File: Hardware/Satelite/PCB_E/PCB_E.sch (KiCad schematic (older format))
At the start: 15 parts, among them J1 Conn_02x02_Counter_Clockwise, J12 Conector_Expansion_CanSat, J14 Conn_01x06, J15 Conn_01x06, J2 Conn_02x02_Counter_Clockwise, J3 Conn_02x02_Counter_Clockwise, J4 Conn_02x10_Odd_Even, J5 Conn_02x10_Odd_Even, J6 Conn_02x10_Odd_Even, J7 Conn_02x10_Odd_Even, J8 Conn_01x06, M1 Spacer, M2 Spacer, M3 Spacer

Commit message: Espaciadores más largos para PCB que usan conector de expansión
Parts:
- J12: symbol AXTEC_IC:Conector_Expansion_CanSat -> PCB_E-rescue:Conector_Expansion_CanSat-AXTEC_IC
- M1, M2, M3: symbol AXTEC_IC:Spacer -> PCB_E-rescue:Spacer-AXTEC_IC; Manufacturer Part Number R30-3011002 -> R30-3011202
- MH1: symbol AXTEC_IC:MH_CanSat -> PCB_E-rescue:MH_CanSat-AXTEC_IC
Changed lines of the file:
@@
 EESchema Schematic File Version 4
 LIBS:PCB_E-cache
-EELAYER 26 0
+EELAYER 29 0
 EELAYER END
 $Descr A4 11693 8268
@@
 IO6
 $Comp
-L AXTEC_IC:MH_CanSat MH1
+L PCB_E-rescue:MH_CanSat-AXTEC_IC MH1
 U 1 1 5BC69FBC
 P 5250 4650
@@
 	8050 2150 8050 2250
 $Comp
-L AXTEC_IC:Spacer M1
+L PCB_E-rescue:Spacer-AXTEC_IC M1
 U 1 1 5C332544
 P 4400 5450
@@
 F 2 "AXTEC:Empty_Footprint" H 4300 5600 50  0001 C CNN
 F 3 "https://www.mouser.com/datasheet/2/181/R30-301-1135805.pdf" H 4400 5700 50  0001 C CNN
-F 4 "R30-3011002" H 4479 5305 50  0001 L CNN "Manufacturer Part Number"
+F 4 "R30-3011202" H 4479 5305 50  0001 L CNN "Manufacturer Part Number"
 	1    4400 5450
 	1    0    0    -1
 $EndComp
 $Comp
-L AXTEC_IC:Spacer M2
+L PCB_E-rescue:Spacer-AXTEC_IC M2
 U 1 1 5C332635
 P 5250 5450
@@
 F 2 "AXTEC:Empty_Footprint" H 5150 5600 50  0001 C CNN
 F 3 "https://www.mouser.com/datasheet/2/181/R30-301-1135805.pdf" H 5250 5700 50  0001 C CNN
-F 4 "R30-3011002" H 5329 5305 50  0001 L CNN "Manufacturer Part Number"
+F 4 "R30-3011202" H 5329 5305 50  0001 L CNN "Manufacturer Part Number"
 	1    5250 5450
 	1    0    0    -1
 $EndComp
 $Comp
-L AXTEC_IC:Spacer M3
+L PCB_E-rescue:Spacer-AXTEC_IC M3
 U 1 1 5C332687
 P 6000 5450
@@
 F 2 "AXTEC:Empty_Footprint" H 5900 5600 50  0001 C CNN
 F 3 "https://www.mouser.com/datasheet/2/181/R30-301-1135805.pdf" H 6000 5700 50  0001 C CNN
-F 4 "R30-3011002" H 6079 5305 50  0001 L CNN "Manufacturer Part Number"
+F 4 "R30-3011202" H 6079 5305 50  0001 L CNN "Manufacturer Part Number"
 	1    6000 5450
 	1    0    0    -1
@@
 $EndComp
 $Comp
-L AXTEC_IC:Conector_Expansion_CanSat J12
+L PCB_E-rescue:Conector_Expansion_CanSat-AXTEC_IC J12
 U 1 1 5C26BB39
 P 8750 2100

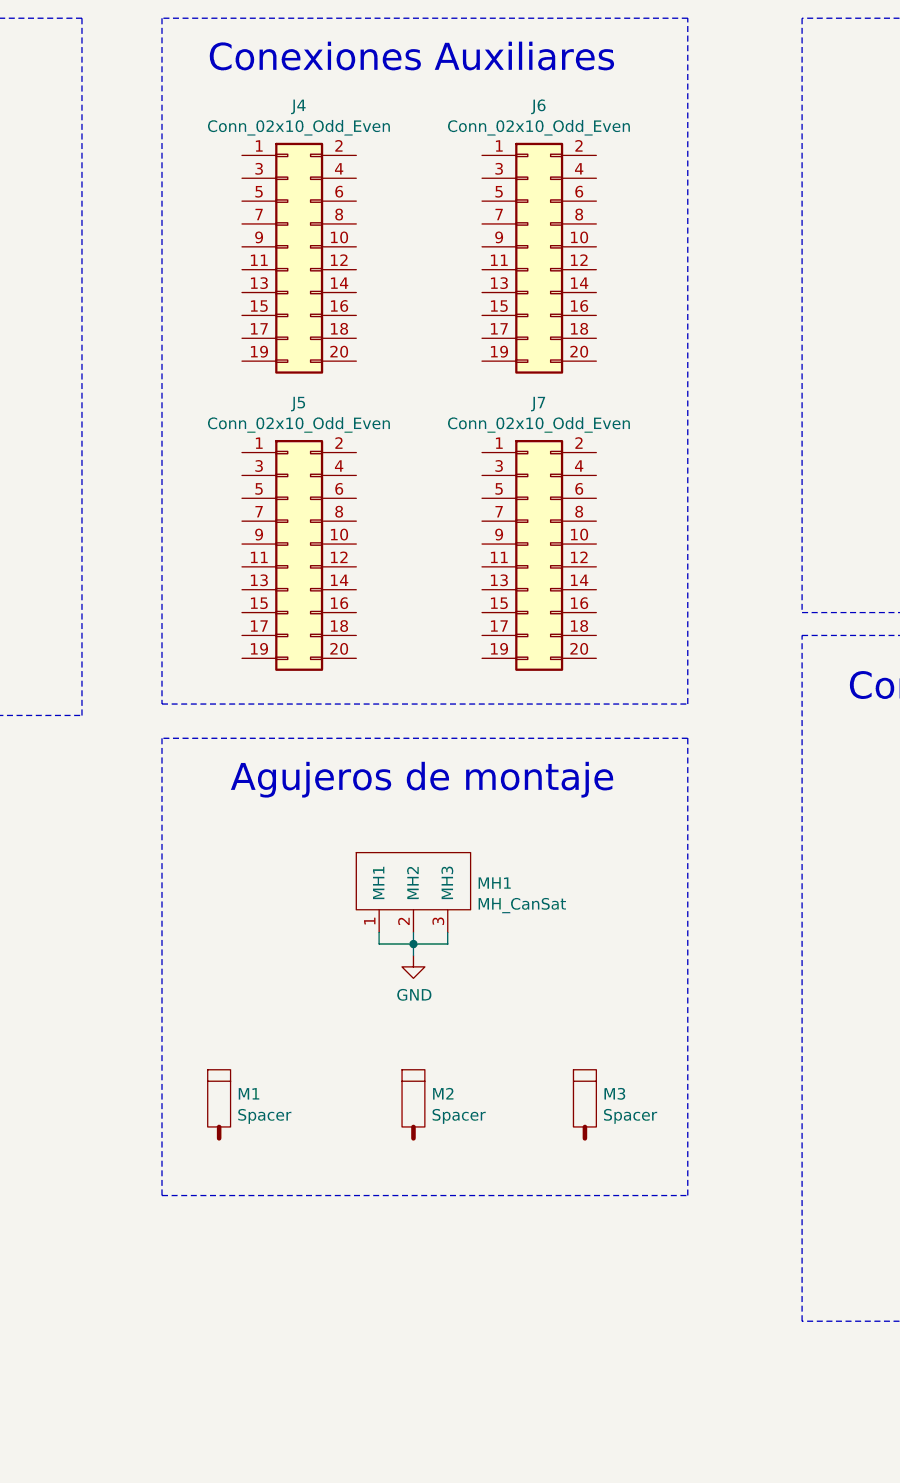
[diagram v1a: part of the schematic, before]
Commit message: Agregado más pines y corrección de distancia entre pines en PCB_E
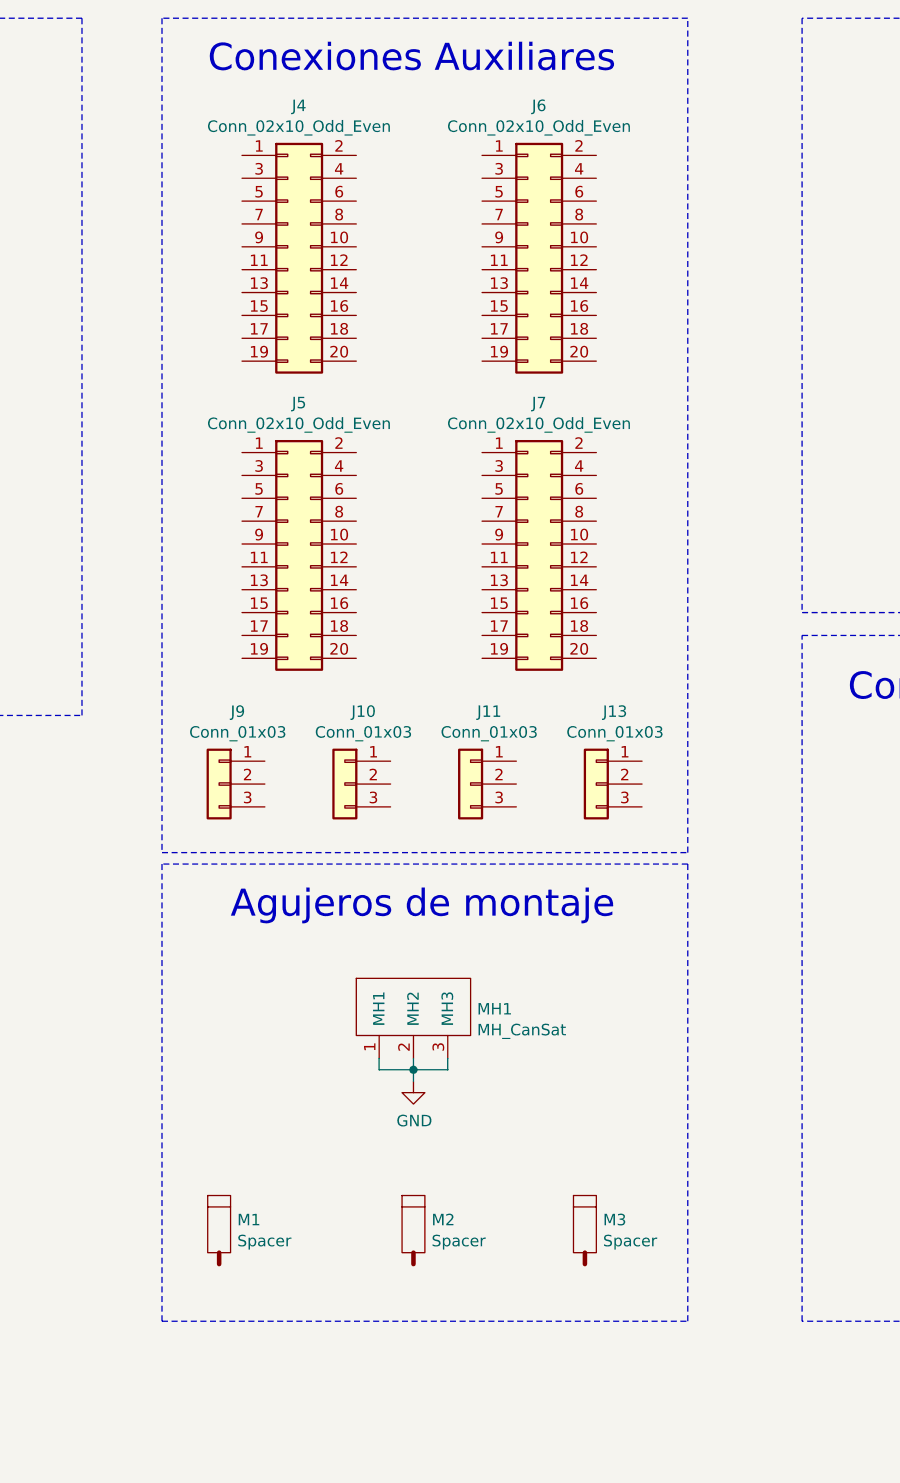
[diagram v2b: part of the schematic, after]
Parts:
- added J10, J11, J13, J9: Conn_01x03, Connector_PinHeader_2.54mm:PinHeader_1x03_P2.54mm_Vertical, symbol Connector_Generic:Conn_01x03
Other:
- moved on the sheet: M1, M2, M3, MH1
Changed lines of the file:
@@
 $EndComp
 Wire Notes Line
-	4150 750  4150 3750
-Wire Notes Line
-	4150 3750 6450 3750
-Wire Notes Line
-	6450 3750 6450 750
+	4150 750  4150 4400
+Wire Notes Line
+	4150 4400 6450 4400
+Wire Notes Line
+	6450 4400 6450 750
 Wire Notes Line
 	6450 750  4150 750
@@
 L power:GND #PWR07
 U 1 1 5BC9E797
-P 5250 4850
-F 0 "#PWR07" H 5250 4600 50  0001 C CNN
-F 1 "GND" H 5254 4676 50  0000 C CNN
-F 2 "" H 5250 4850 50  0001 C CNN
-F 3 "" H 5250 4850 50  0001 C CNN
-	1    5250 4850
+P 5250 5400
+F 0 "#PWR07" H 5250 5150 50  0001 C CNN
+F 1 "GND" H 5254 5226 50  0000 C CNN
+F 2 "" H 5250 5400 50  0001 C CNN
+F 3 "" H 5250 5400 50  0001 C CNN
+	1    5250 5400
 	1    0    0    -1
 $EndComp
@@
 L PCB_E-rescue:MH_CanSat-AXTEC_IC MH1
 U 1 1 5BC69FBC
-P 5250 4650
-F 0 "MH1" H 5528 4765 50  0000 L CNN
-F 1 "MH_CanSat" H 5528 4674 50  0000 L CNN
-F 2 "AXTEC:MH_CanSat" H 5250 4650 50  0001 C CNN
-F 3 "" H 5250 4650 50  0001 C CNN
-	1    5250 4650
-	1    0    0    -1
-$EndComp
-Wire Wire Line
-	5100 4750 5100 4800
-Wire Wire Line
-	5100 4800 5250 4800
-Wire Wire Line
-	5400 4800 5400 4750
-Wire Wire Line
-	5250 4750 5250 4800
-Connection ~ 5250 4800
-Wire Wire Line
-	5250 4800 5400 4800
-Wire Wire Line
-	5250 4850 5250 4800
-Wire Notes Line
-	4150 3900 4150 5900
-Wire Notes Line
-	4150 5900 6450 5900
-Wire Notes Line
-	6450 5900 6450 3900
-Wire Notes Line
-	6450 3900 4150 3900
-Text Notes 4450 4150 0    118  ~ 0
+P 5250 5200
+F 0 "MH1" H 5528 5315 50  0000 L CNN
+F 1 "MH_CanSat" H 5528 5224 50  0000 L CNN
+F 2 "AXTEC:MH_CanSat" H 5250 5200 50  0001 C CNN
+F 3 "" H 5250 5200 50  0001 C CNN
+	1    5250 5200
+	1    0    0    -1
+$EndComp
+Wire Wire Line
+	5100 5300 5100 5350
+Wire Wire Line
+	5100 5350 5250 5350
+Wire Wire Line
+	5400 5350 5400 5300
+Wire Wire Line
+	5250 5300 5250 5350
+Connection ~ 5250 5350
+Wire Wire Line
+	5250 5350 5400 5350
+Wire Wire Line
+	5250 5400 5250 5350
+Wire Notes Line
+	4150 4450 4150 6450
+Wire Notes Line
+	4150 6450 6450 6450
+Wire Notes Line
+	6450 6450 6450 4450
+Wire Notes Line
+	6450 4450 4150 4450
+Text Notes 4450 4700 0    118  ~ 0
 Agujeros de montaje
 Wire Wire Line
@@
 L PCB_E-rescue:Spacer-AXTEC_IC M1
 U 1 1 5C332544
-P 4400 5450
-F 0 "M1" H 4479 5443 50  0000 L CNN
-F 1 "Spacer" H 4479 5351 50  0000 L CNN
-F 2 "AXTEC:Empty_Footprint" H 4300 5600 50  0001 C CNN
-F 3 "https://www.mouser.com/datasheet/2/181/R30-301-1135805.pdf" H 4400 5700 50  0001 C CNN
-F 4 "R30-3011202" H 4479 5305 50  0001 L CNN "Manufacturer Part Number"
-	1    4400 5450
+P 4400 6000
+F 0 "M1" H 4479 5993 50  0000 L CNN
+F 1 "Spacer" H 4479 5901 50  0000 L CNN
+F 2 "AXTEC:Empty_Footprint" H 4300 6150 50  0001 C CNN
+F 3 "https://www.mouser.com/datasheet/2/181/R30-301-1135805.pdf" H 4400 6250 50  0001 C CNN
+F 4 "R30-3011202" H 4479 5855 50  0001 L CNN "Manufacturer Part Number"
+	1    4400 6000
 	1    0    0    -1
 $EndComp
@@
 L PCB_E-rescue:Spacer-AXTEC_IC M2
 U 1 1 5C332635
-P 5250 5450
-F 0 "M2" H 5329 5443 50  0000 L CNN
-F 1 "Spacer" H 5329 5351 50  0000 L CNN
-F 2 "AXTEC:Empty_Footprint" H 5150 5600 50  0001 C CNN
-F 3 "https://www.mouser.com/datasheet/2/181/R30-301-1135805.pdf" H 5250 5700 50  0001 C CNN
-F 4 "R30-3011202" H 5329 5305 50  0001 L CNN "Manufacturer Part Number"
-	1    5250 5450
+P 5250 6000
+F 0 "M2" H 5329 5993 50  0000 L CNN
+F 1 "Spacer" H 5329 5901 50  0000 L CNN
+F 2 "AXTEC:Empty_Footprint" H 5150 6150 50  0001 C CNN
+F 3 "https://www.mouser.com/datasheet/2/181/R30-301-1135805.pdf" H 5250 6250 50  0001 C CNN
+F 4 "R30-3011202" H 5329 5855 50  0001 L CNN "Manufacturer Part Number"
+	1    5250 6000
 	1    0    0    -1
 $EndComp
@@
 L PCB_E-rescue:Spacer-AXTEC_IC M3
 U 1 1 5C332687
-P 6000 5450
-F 0 "M3" H 6079 5443 50  0000 L CNN
-F 1 "Spacer" H 6079 5351 50  0000 L CNN
-F 2 "AXTEC:Empty_Footprint" H 5900 5600 50  0001 C CNN
-F 3 "https://www.mouser.com/datasheet/2/181/R30-301-1135805.pdf" H 6000 5700 50  0001 C CNN
-F 4 "R30-3011202" H 6079 5305 50  0001 L CNN "Manufacturer Part Number"
-	1    6000 5450
+P 6000 6000
+F 0 "M3" H 6079 5993 50  0000 L CNN
+F 1 "Spacer" H 6079 5901 50  0000 L CNN
+F 2 "AXTEC:Empty_Footprint" H 5900 6150 50  0001 C CNN
+F 3 "https://www.mouser.com/datasheet/2/181/R30-301-1135805.pdf" H 6000 6250 50  0001 C CNN
+F 4 "R30-3011202" H 6079 5855 50  0001 L CNN "Manufacturer Part Number"
+	1    6000 6000
 	1    0    0    -1
 $EndComp
@@
 Text Label 9650 4100 0    50   ~ 0
 IO5
+$Comp
+L Connector_Generic:Conn_01x03 J9
+U 1 1 5CDCF65D
+P 4400 4100
+F 0 "J9" H 4318 4417 50  0000 C CNN
+F 1 "Conn_01x03" H 4318 4326 50  0000 C CNN
+F 2 "Connector_PinHeader_2.54mm:PinHeader_1x03_P2.54mm_Vertical" H 4400 4100 50  0001 C CNN
+F 3 "~" H 4400 4100 50  0001 C CNN
+	1    4400 4100
+	-1   0    0    -1
+$EndComp
+$Comp
+L Connector_Generic:Conn_01x03 J10
+U 1 1 5CDD16C8
+P 4950 4100
+F 0 "J10" H 4868 4417 50  0000 C CNN
+F 1 "Conn_01x03" H 4868 4326 50  0000 C CNN
+F 2 "Connector_PinHeader_2.54mm:PinHeader_1x03_P2.54mm_Vertical" H 4950 4100 50  0001 C CNN
+F 3 "~" H 4950 4100 50  0001 C CNN
+	1    4950 4100
+	-1   0    0    -1
+$EndComp
+$Comp
+L Connector_Generic:Conn_01x03 J11
+U 1 1 5CDD1C29
+P 5500 4100
+F 0 "J11" H 5418 4417 50  0000 C CNN
+F 1 "Conn_01x03" H 5418 4326 50  0000 C CNN
+F 2 "Connector_PinHeader_2.54mm:PinHeader_1x03_P2.54mm_Vertical" H 5500 4100 50  0001 C CNN
+F 3 "~" H 5500 4100 50  0001 C CNN
+	1    5500 4100
+	-1   0    0    -1
+$EndComp
+$Comp
+L Connector_Generic:Conn_01x03 J13
+U 1 1 5CDD2034
+P 6050 4100
+F 0 "J13" H 5968 4417 50  0000 C CNN
+F 1 "Conn_01x03" H 5968 4326 50  0000 C CNN
+F 2 "Connector_PinHeader_2.54mm:PinHeader_1x03_P2.54mm_Vertical" H 6050 4100 50  0001 C CNN
+F 3 "~" H 6050 4100 50  0001 C CNN
+	1    6050 4100
+	-1   0    0    -1
+$EndComp
 $EndSCHEMATC

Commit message: PCB_E BOM
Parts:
- J12: Manufacturer Part Number (none) -> SSQ-106-03-T-S; Quantity (none) -> 4
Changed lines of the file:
@@
 F 2 "AXTEC:Conector_Expansion_CanSat" H 8750 2600 50  0001 C CNN
 F 3 "" H 8750 2600 50  0001 C CNN
+F 4 "SSQ-106-03-T-S" H 8750 2100 50  0001 C CNN "Manufacturer Part Number"
+F 5 "4" H 8750 2100 50  0001 C CNN "Quantity"
 	1    8750 2100
 	1    0    0    -1
